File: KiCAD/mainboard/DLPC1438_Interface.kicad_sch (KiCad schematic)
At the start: 81 parts, among them IC1 DLPC1438ZEZ, IC14 SN74AUP1G06DCKR, IC6 SN74AUP1G06DCKR, J2 Conn_01x07_Pin, J3 Conn_02x05_Odd_Even, J31 Conn_01x08_Pin, J4 Conn_01x05_Pin, U12 ECS-2520MV-xxx-xx, U13 MX25L3233FM2, U22 TXS0102DCU, U7 SN74AUP1G06DCKR

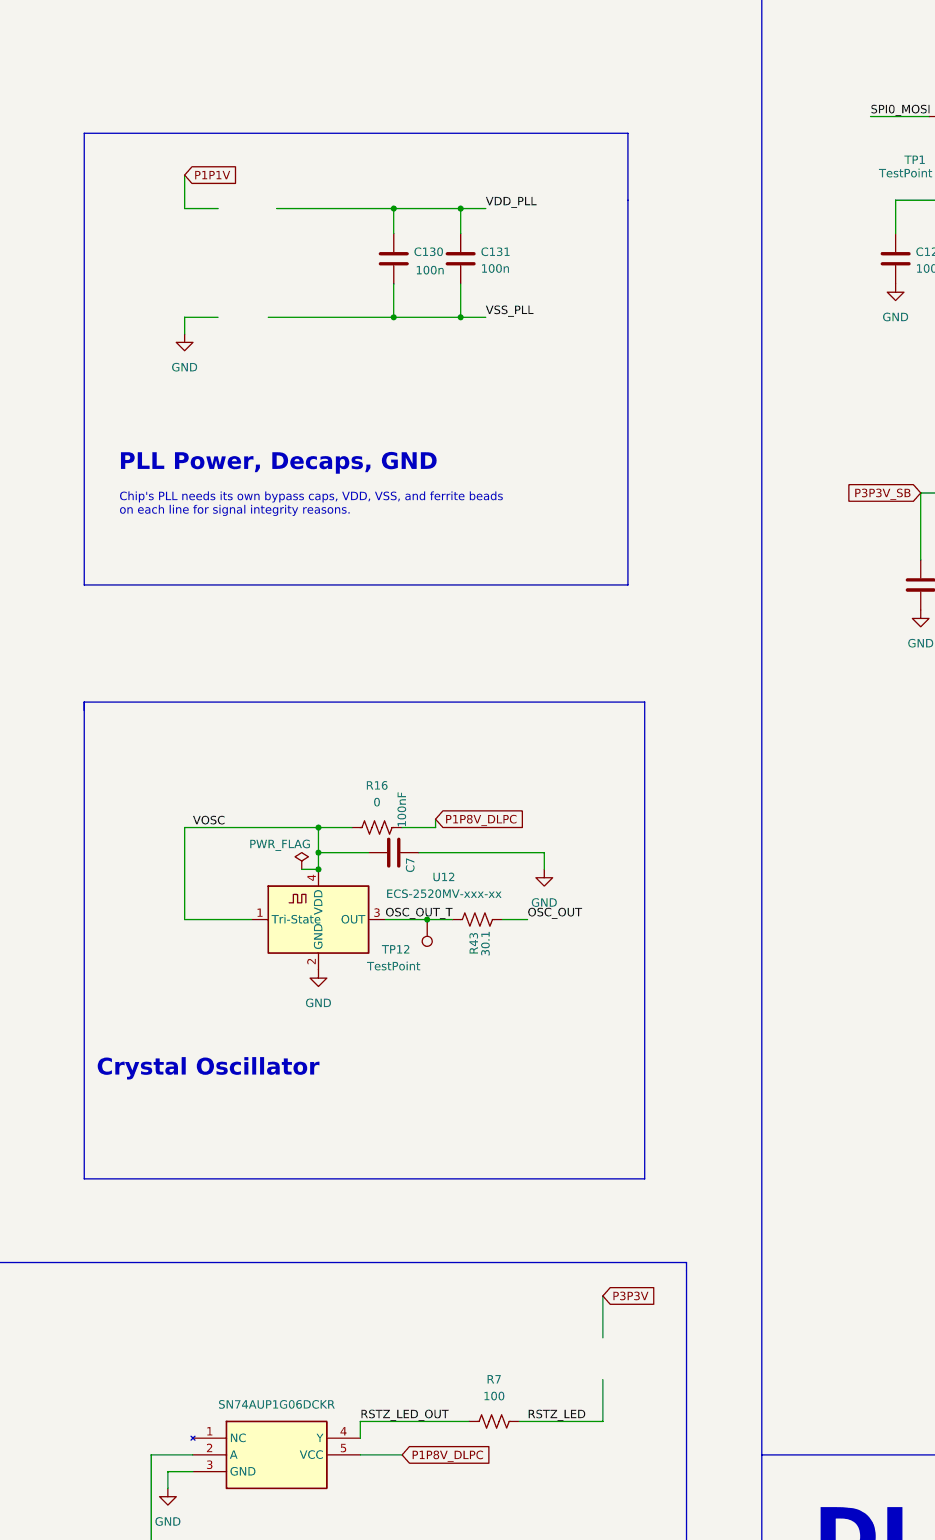
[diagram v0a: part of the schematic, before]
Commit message: added libraries and symbols and step for ferrite beads and D7 LED
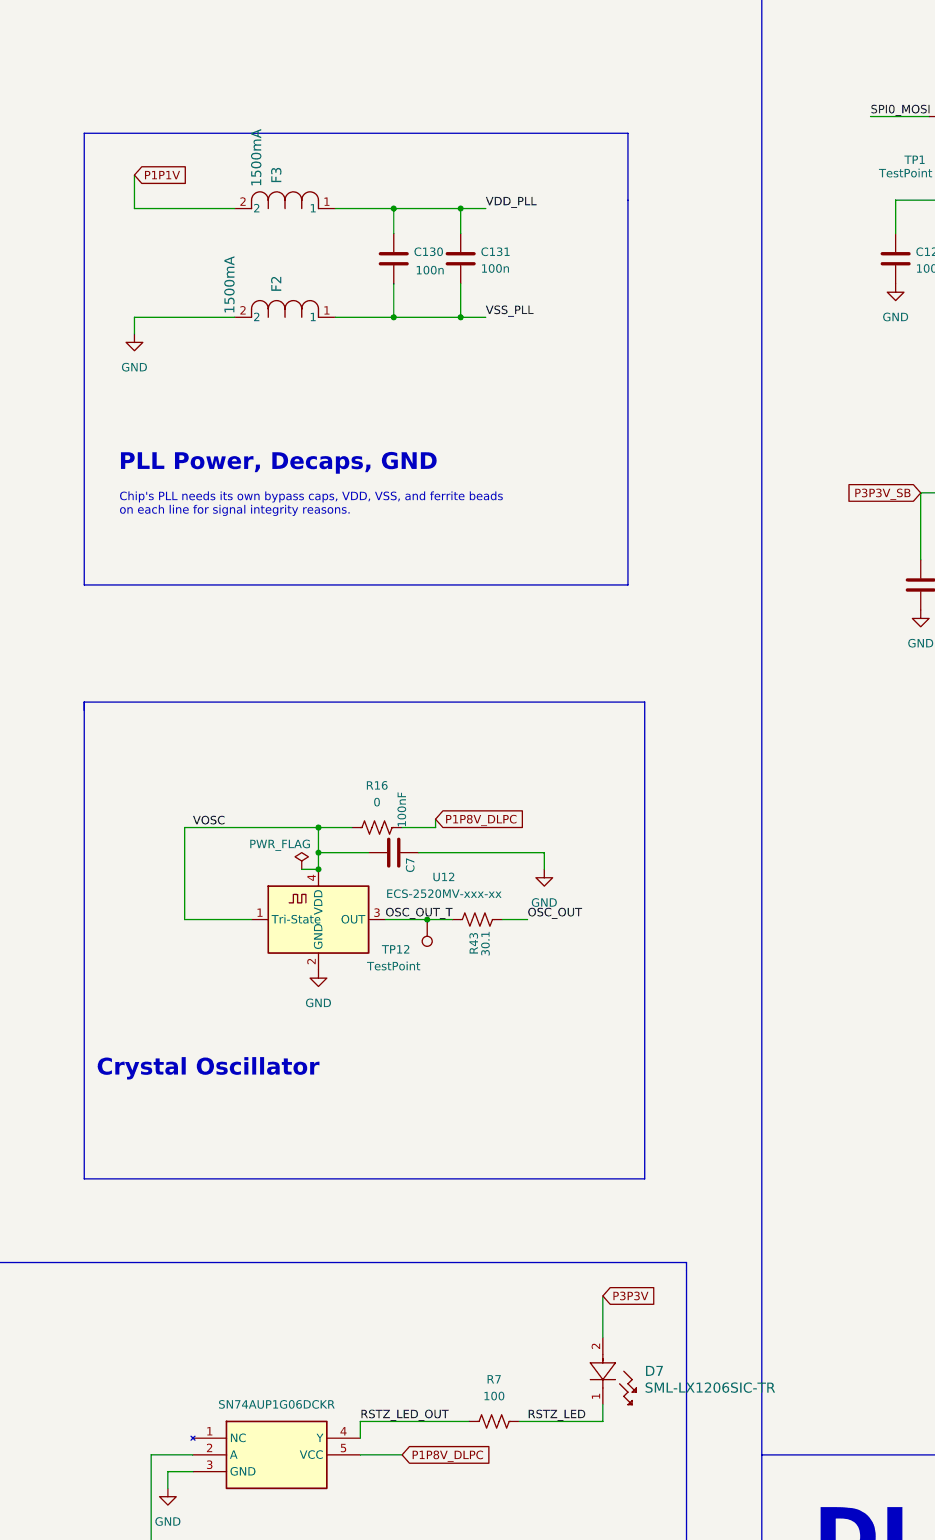
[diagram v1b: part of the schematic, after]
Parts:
- added D7: SML-LX1206SIC-TR, tp_library:LED_SML-LX1206SIC-TR_LUM-M, symbol ul_SML-LX1206SIC-TR:SML-LX1206SIC-TR
- added F2, F3: 1500mA, tp_library:BLM15P_FBD-M, symbol BLM15P_FBD-M:BLM15PD800SN1D
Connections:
- net GND: now also F2.2
- net P1P1V: now also F3.2
- net P3P3V: now also D7.2
- net RSTZ_LED: now also D7.1
- net VDD_PLL: now also F3.1
- net VSS_PLL: now also F2.1
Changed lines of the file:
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@@
 	(wire
 		(pts
-			(xy 210.82 127) (xy 215.9 127)
+			(xy 203.2 127) (xy 218.44 127)
 		)
 		(stroke
@@
 	(wire
 		(pts
-			(xy 224.79 127) (xy 242.57 127)
+			(xy 233.68 127) (xy 242.57 127)
 		)
 		(stroke
@@
 	(wire
 		(pts
-			(xy 274.32 304.8) (xy 274.32 311.15)
-		)
-		(stroke
-			(width 0)
-			(type default)
-		)
-	)
-	(wire
-		(pts
 			(xy 534.67 345.44) (xy 533.4 345.44)
 		)
@@
 	(wire
 		(pts
-			(xy 210.82 143.51) (xy 210.82 146.05)
+			(xy 203.2 143.51) (xy 203.2 146.05)
 		)
 		(stroke
@@
 	(wire
 		(pts
-			(xy 215.9 143.51) (xy 210.82 143.51)
+			(xy 218.44 143.51) (xy 203.2 143.51)
 		)
 		(stroke
@@
 	(wire
 		(pts
+			(xy 274.32 292.1) (xy 274.32 298.45)
+		)
+		(stroke
+			(width 0)
+			(type default)
+		)
+	)
+	(wire
+		(pts
 			(xy 417.83 250.19) (xy 421.64 250.19)
 		)
@@
 	(wire
 		(pts
-			(xy 210.82 121.92) (xy 210.82 127)
+			(xy 203.2 121.92) (xy 203.2 127)
 		)
 		(stroke
@@
 	(wire
 		(pts
-			(xy 431.8 49.53) (xy 431.8 64.77)
+			(xy 274.32 308.61) (xy 274.32 311.15)
 		)
 		(stroke
@@
 	(wire
 		(pts
-			(xy 186.69 60.96) (xy 186.69 66.04)
+			(xy 431.8 49.53) (xy 431.8 64.77)
 		)
 		(stroke
@@
 	(wire
 		(pts
-			(xy 201.93 66.04) (xy 210.82 66.04)
+			(xy 186.69 60.96) (xy 186.69 66.04)
 		)
 		(stroke
@@
 	(wire
 		(pts
-			(xy 513.08 342.9) (xy 510.54 342.9)
+			(xy 201.93 66.04) (xy 210.82 66.04)
 		)
 		(stroke
@@
 		)
 	)
-	(polyline
+	(wire
 		(pts
-			(xy 170.18 273.05) (xy 20.32 273.05)
+			(xy 513.08 342.9) (xy 510.54 342.9)
 		)
 		(stroke
@@
 		)
 	)
-	(wire
+	(polyline
 		(pts
-			(xy 492.76 68.58) (xy 528.32 68.58)
+			(xy 170.18 273.05) (xy 20.32 273.05)
 		)
 		(stroke
@@
 	(wire
 		(pts
-			(xy 274.32 292.1) (xy 274.32 298.45)
+			(xy 492.76 68.58) (xy 528.32 68.58)
 		)
 		(stroke
@@
 	(wire
 		(pts
-			(xy 223.52 143.51) (xy 242.57 143.51)
+			(xy 233.68 143.51) (xy 242.57 143.51)
 		)
 		(stroke
@@
 	(global_label "P1P1V"
 		(shape input)
-		(at 210.82 121.92 0)
+		(at 203.2 121.92 0)
 		(fields_autoplaced yes)
 		(effects
@@
 		)
 		(property "Intersheetrefs" "${INTERSHEET_REFS}"
-			(at 219.8528 121.92 0)
+			(at 212.2328 121.92 0)
 			(effects
 				(font
@@
 	)
 	(symbol
+		(lib_id "BLM15P_FBD-M:BLM15PD800SN1D")
+		(at 218.44 127 270)
+		(unit 1)
+		(exclude_from_sim no)
+		(in_bom yes)
+		(on_board yes)
+		(dnp no)
+		(property "Reference" "F3"
+			(at 224.7899 123.19 0)
+			(effects
+				(font
+					(size 1.524 1.524)
+				)
+				(justify right)
+			)
+		)
+		(property "Value" "1500mA"
+			(at 221.742 123.698 0)
+			(effects
+				(font
+					(size 1.524 1.524)
+				)
+				(justify right)
+			)
+		)
+		(property "Footprint" "tp_library:BLM15P_FBD-M"
+			(at 218.44 127 0)
+			(effects
+				(font
+					(size 1.27 1.27)
+					(italic yes)
+				)
+				(hide yes)
+			)
+		)
+		(property "Datasheet" "BLM15PD800SN1D"
+			(at 218.44 127 0)
+			(effects
+				(font
+					(size 1.27 1.27)
+					(italic yes)
+				)
+				(hide yes)
+			)
+		)
+		(property "Description" ""
+			(at 218.44 127 0)
+			(effects
+				(font
+					(size 1.27 1.27)
+				)
+				(hide yes)
+			)
+		)
+		(pin "1"
+		)
+		(pin "2"
+		)
+		(instances
+			(project ""
+				(path "/38e83f42-2cf9-4799-a46f-ca415d95b90a/a69a407c-1a7c-4ac9-a9eb-cd67809c5ec0"
+					(reference "F3")
+					(unit 1)
+				)
+			)
+		)
+	)
+	(symbol
 		(lib_id "power:GND")
 		(at 330.2 142.24 0)
@@
 	)
 	(symbol
+		(lib_id "BLM15P_FBD-M:BLM15PD800SN1D")
+		(at 218.44 143.51 270)
+		(unit 1)
+		(exclude_from_sim no)
+		(in_bom yes)
+		(on_board yes)
+		(dnp no)
+		(property "Reference" "F2"
+			(at 224.7899 139.7 0)
+			(effects
+				(font
+					(size 1.524 1.524)
+				)
+				(justify right)
+			)
+		)
+		(property "Value" "1500mA"
+			(at 217.678 143.002 0)
+			(effects
+				(font
+					(size 1.524 1.524)
+				)
+				(justify right)
+			)
+		)
+		(property "Footprint" "tp_library:BLM15P_FBD-M"
+			(at 218.44 143.51 0)
+			(effects
+				(font
+					(size 1.27 1.27)
+					(italic yes)
+				)
+				(hide yes)
+			)
+		)
+		(property "Datasheet" "BLM15PD800SN1D"
+			(at 218.44 143.51 0)
+			(effects
+				(font
+					(size 1.27 1.27)
+					(italic yes)
+				)
+				(hide yes)
+			)
+		)
+		(property "Description" ""
+			(at 218.44 143.51 0)
+			(effects
+				(font
+					(size 1.27 1.27)
+				)
+				(hide yes)
+			)
+		)
+		(pin "1"
+		)
+		(pin "2"
+		)
+		(instances
+			(project "mainboard"
+				(path "/38e83f42-2cf9-4799-a46f-ca415d95b90a/a69a407c-1a7c-4ac9-a9eb-cd67809c5ec0"
+					(reference "F2")
+					(unit 1)
+				)
+			)
+		)
+	)
+	(symbol
 		(lib_id "Connector:Conn_01x05_Pin")
 		(at 547.37 124.46 0)
@@
 	)
 	(symbol
+		(lib_id "ul_SML-LX1206SIC-TR:SML-LX1206SIC-TR")
+		(at 274.32 298.45 270)
+		(unit 1)
+		(exclude_from_sim no)
+		(in_bom yes)
+		(on_board yes)
+		(dnp no)
+		(fields_autoplaced yes)
+		(property "Reference" "D7"
+			(at 280.67 303.5299 90)
+			(effects
+				(font
+					(size 1.524 1.524)
+				)
+				(justify left)
+			)
+		)
+		(property "Value" "SML-LX1206SIC-TR"
+			(at 280.67 306.0699 90)
+			(effects
+				(font
+					(size 1.524 1.524)
+				)
+				(justify left)
+			)
+		)
+		(property "Footprint" "tp_library:LED_SML-LX1206SIC-TR_LUM-M"
+			(at 274.32 298.45 0)
+			(effects
+				(font
+					(size 1.27 1.27)
+					(italic yes)
+				)
+				(hide yes)
+			)
+		)
+		(property "Datasheet" "SML-LX1206SIC-TR"
+			(at 274.32 298.45 0)
+			(effects
+				(font
+					(size 1.27 1.27)
+					(italic yes)
+				)
+				(hide yes)
+			)
+		)
+		(property "Description" ""
+			(at 274.32 298.45 0)
+			(effects
+				(font
+					(size 1.27 1.27)
+				)
+				(hide yes)
+			)
+		)
+		(pin "2"
+		)
+		(pin "1"
+		)
+		(instances
+			(project ""
+				(path "/38e83f42-2cf9-4799-a46f-ca415d95b90a/a69a407c-1a7c-4ac9-a9eb-cd67809c5ec0"
+					(reference "D7")
+					(unit 1)
+				)
+			)
+		)
+	)
+	(symbol
 		(lib_id "Device:C")
 		(at 210.82 57.15 0)
@@
 	(symbol
 		(lib_id "power:GND")
-		(at 210.82 146.05 0)
+		(at 203.2 146.05 0)
 		(unit 1)
 		(exclude_from_sim no)
@@
 		(fields_autoplaced yes)
 		(property "Reference" "#PWR032"
-			(at 210.82 152.4 0)
+			(at 203.2 152.4 0)
 			(effects
 				(font
@@
 		)
 		(property "Value" "GND"
-			(at 210.82 151.13 0)
+			(at 203.2 151.13 0)
 			(effects
 				(font
@@
 		)
 		(property "Footprint" ""
-			(at 210.82 146.05 0)
+			(at 203.2 146.05 0)
 			(effects
 				(font
@@
 		)
 		(property "Datasheet" ""
-			(at 210.82 146.05 0)
+			(at 203.2 146.05 0)
 			(effects
 				(font
@@
 		)
 		(property "Description" "Power symbol creates a global label with name \"GND\" , ground"
-			(at 210.82 146.05 0)
+			(at 203.2 146.05 0)
 			(effects
 				(font

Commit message: added sym mod and step for resistors but package 0805
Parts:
- removed R1: 10k, Resistor_SMD:R_0805_2012Metric_Pad1.20x1.40mm_HandSolder, symbol Device:R_US
- removed R3: 100k, Resistor_SMD:R_0805_2012Metric_Pad1.20x1.40mm_HandSolder, symbol Device:R_US
- added R1: 10k, tp_library:STA_RMCF0805_STP-M, symbol RMCF0805FT10K0:RMCF0805FT10K0
- added R8: 100, tp_library:RES_CRCW_0805-M, symbol CRCW0805100RFKEA:CRCW0805100RFKEA
- added R9: 30.1, RC0805FR-0730R1L:RESC2012X60N, symbol RC0805FR-0730R1L:RC0805FR-0730R1L
- C112, C114, C115, C170, C171, C7: value 100nF -> 100n; footprint Capacitor_SMD:C_0805_2012Metric_Pad1.18x1.45mm_HandSolder -> Capacitor_SMD:C_0402_1005Metric; Manufacturer_Part_Number (none) -> CL05B104KO5NNNC
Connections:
- net GND: now also C115.1, C170.2, C171.1, C7.1; no longer C115.2, C170.1, C171.2, C7.2
- net P1P8V_DLPC: now also C170.1; no longer C170.2
- net P3P3V: now also C171.2; no longer C171.1
- net P3P3V_SB: now also C115.2; no longer C115.1
- net VOSC: now also C7.2; no longer C7.1

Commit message: replaced with 0805 all passives in DLPC
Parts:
- removed R1: 10k, tp_library:STA_RMCF0805_STP-M, symbol RMCF0805FT10K0:RMCF0805FT10K0
- removed R2: 100, Resistor_SMD:R_0805_2012Metric_Pad1.20x1.40mm_HandSolder, symbol Device:R_US
- removed R8: 100, tp_library:RES_CRCW_0805-M, symbol CRCW0805100RFKEA:CRCW0805100RFKEA
- removed R9: 30.1, RC0805FR-0730R1L:RESC2012X60N, symbol RC0805FR-0730R1L:RC0805FR-0730R1L
- C112, C114, C115, C120, C121, C125, C126, C127, C128, C129, C130, C131, C132, C133, C134, C138, C139, C140, C141, C142, C143, C144, C145, C155, C156, C157, C170, C171, C7: footprint Capacitor_SMD:C_0402_1005Metric -> CC0805KRX7R9BB104:CAPC2012X70; symbol Device:C -> CC0805KRX7R9BB104:CC0805KRX7R9BB104; Check_prices (none) -> https://www.snapeda.com/parts/CC0805KRX7R9BB104/Yageo/view-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; Description_1 (none) -> 0.1 µF ±10% 50V Ceramic Capacitor X7R 0805 (2012 Metric); DigiKey_Part_Number (none) -> 311-1140-1-ND; MANUFACTURER (none) -> YAGEO; MF (none) -> Yageo; MP (none) -> CC0805KRX7R9BB104; Package (none) -> 0805 Yageo; SnapEDA_Link (none) -> https://www.snapeda.com/parts/CC0805KRX7R9BB104/Yageo/view-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
- R16, R171: footprint Resistor_SMD:R_0805_2012Metric_Pad1.20x1.40mm_HandSolder -> RES_R-070RL_VIS; symbol Device:R_US -> RC0805JR-070RL:RC0805JR-070RL; Manufacturer_Part_Number (none) -> RC0805JR-070RL
- R163, R164, R165, R170, R92: footprint Resistor_SMD:R_0805_2012Metric_Pad1.20x1.40mm_HandSolder -> STA_RMCF0805_STP; symbol Device:R_US -> RMCF0805FT10K0:RMCF0805FT10K0; Manufacturer_Part_Number (none) -> RMCF0805FT10K0
- R166: footprint Resistor_SMD:R_0402_1005Metric -> STA_RMCF0805_STP; symbol Device:R_US -> RMCF0805FT10K0:RMCF0805FT10K0; Manufacturer_Part_Number CRCW0402100KFKED -> RMCF0805FT10K0
- R168, R17, R174, R19: footprint Resistor_SMD:R_0805_2012Metric_Pad1.20x1.40mm_HandSolder -> RES_RMCF0805_STP; symbol Device:R_US -> RMCF0805FG100K:RMCF0805FG100K; Manufacturer_Part_Number (none) -> RMCF0805FG100K
- R172, R173, R18, R43, R76: footprint Resistor_SMD:R_0805_2012Metric_Pad1.20x1.40mm_HandSolder -> RC0805FR-0730R1L:RESC2012X60N; symbol Device:R_US -> RC0805FR-0730R1L:RC0805FR-0730R1L; Check_prices (none) -> https://www.snapeda.com/parts/RC0805FR-0730R1L/Yageo/view-p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; Description_1 (none) -> 30.1 Ohms ±1% 0.125W, 1/8W Chip Resistor 0805 (2012 Metric)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; DigiKey_Part_Number (none) -> 311-30.1CRCT-ND; MF (none) -> Yageo; MP (none) -> RC0805FR-0730R1L; Manufacturer_Part_Number (none) -> RC0805FR-0730R1L; Package (none) -> 2012 Yageo; SnapEDA_Link (none) -> https://www.snapeda.com/parts/RC0805FR-0730R1L/Yageo/view-p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
- R176, R177, R178, R179: footprint Resistor_SMD:R_0402_1005Metric -> RES_RMCF0805_STP; symbol Device:R_US -> RMCF0805FG100K:RMCF0805FG100K; Manufacturer_Part_Number CRCW0402100KFKED -> RMCF0805FG100K
- R42, R52: footprint Resistor_SMD:R_0402_1005Metric -> RES_RM10_CCE; symbol Device:R_US -> RM10F7871CT:RM10F7871CT
- R5, R7: footprint Resistor_SMD:R_0805_2012Metric_Pad1.20x1.40mm_HandSolder -> RES_CRCW_0805; symbol Device:R_US -> CRCW0805100RFKEA:CRCW0805100RFKEA; Manufacturer_Part_Number (none) -> CRCW0805100RFKEA
- R53, R54, R55, R73: footprint Resistor_SMD:R_0805_2012Metric_Pad1.20x1.40mm_HandSolder -> RES_ERJP06_PAN; symbol Device:R_US -> ERJP06F3301V:ERJP06F3301V
- R74, R75, R77: footprint RC0402FR-0730R1L -> RC0805FR-0730R1L:RESC2012X60N; symbol Device:R_US -> RC0805FR-0730R1L:RC0805FR-0730R1L; Check_prices (none) -> https://www.snapeda.com/parts/RC0805FR-0730R1L/Yageo/view-p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; Description_1 (none) -> 30.1 Ohms ±1% 0.125W, 1/8W Chip Resistor 0805 (2012 Metric)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; DigiKey_Part_Number (none) -> 311-30.1CRCT-ND; MF (none) -> Yageo; MP (none) -> RC0805FR-0730R1L; Manufacturer_Part_Number RC0402FR-0730R1L -> RC0805FR-0730R1L; Package (none) -> 2012 Yageo; SnapEDA_Link (none) -> https://www.snapeda.com/parts/RC0805FR-0730R1L/Yageo/view-p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
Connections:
- net DLPC_FLSH_PROG: now also R163.1; no longer R163.2, R165.1
- net GND: now also C121.1, C129.1, C133.1, C134.1, C144.1, C145.1, R164.1, R165.1, R174.1, R177.2, R178.2, R179.2, R19.1; no longer C112.2, C114.1, C115.1, C120.2, C121.2, C125.2, C126.2, C127.2, C128.2, C129.2, C132.2, C133.2, C134.2, C138.2, C139.2, C140.2, C141.2, C142.2, C143.2, C144.2, C145.2, C155.2, C156.2, C157.2, C170.2, C171.1, C7.1, R164.2, R165.2, R174.2, R178.1, R179.1, R19.2
- net I2C1_33_EN: no longer R92.2, U22.6 (OE)
- net JTAG_TRSTZ: now also R164.2; no longer R164.1
- net P1P1V: no longer C120.1, C125.1, C126.1, C127.1, C128.1, C132.1, C139.1, C140.1, C141.1, C142.1, C143.1, C155.1
- net P1P8V_DLPC: now also C121.2, C129.2, C133.2, C134.2, C144.2, C145.2; no longer C112.1, C114.2, C121.1, C129.1, C133.1, C134.1, C144.1, C145.1, C156.1, C157.1, C170.1, R177.2
- net P3P3V: now also R5.1; no longer C171.2, R5.2
- net P3P3V_SB: no longer C115.2, C138.1
- net RSTZ_LED: now also R7.1; no longer R7.2
- net RSTZ_LED_OUT: now also R7.2; no longer R7.1
- net SPI0_5V: now also R163.2; no longer R163.1
- net SPI0_CLK: now also R19.2; no longer R19.1
- net SPI0_MOSI: now also R165.2
- net SPI1_MISO: now also R179.1; no longer R179.2
- net SPI1_MOSI: now also R178.1; no longer R178.2
- net VDD_PLL: no longer C130.1, C131.1
- net VOSC: no longer C7.2
- net VSS_PLL: no longer C130.2, C131.2
- net at R171.2, TP21.1: now also R174.2; no longer R174.1
- net at IC6.4 (Y): now also R5.2; no longer R5.1
- new net: R92.2, U22.6 (OE)
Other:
- moved on the sheet: TP21

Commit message: capacitors placed back in place
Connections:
- net GND: now also C112.1, C115.2, C120.1, C125.1, C126.1, C127.1, C128.1, C132.1, C139.1, C140.1, C141.1, C142.1, C143.1, C155.1, C156.1, C157.1, C170.1, C171.2, C7.2
- net P1P1V: now also C120.2, C125.2, C126.2, C127.2, C128.2, C132.2, C139.2, C140.2, C141.2, C142.2, C143.2, C155.2
- net P1P8V_DLPC: now also C112.2, C156.2, C157.2, C170.2
- net P3P3V: now also C171.1
- net P3P3V_SB: now also C115.1
- net VDD_PLL: now also C130.2, C131.2
- net VOSC: now also C7.1
- net VSS_PLL: now also C130.1, C131.1
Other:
- moved on the sheet: C112, C115, C120, C125, C126, C127, C128, C130, C131, C132, C138, C139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

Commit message: changes to all schematic files fixing ERC errors
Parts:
- added R171: 0, RES_R-070RL_VIS, symbol RC0805JR-070RL:RC0805JR-070RL
- added R174: 100k, RES_RMCF0805_STP, symbol RMCF0805FG100K:RMCF0805FG100K
- renumbered TP1 to TP20, IC1 to U16
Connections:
- net DLPC_LED_SEL_1: now also R171.2
- net GND: now also C114.2, C138.1, R174.1; no longer R177.2
- net GPIO_3: now also R177.2
- net I2C1_33_EN: now also R92.2, U22.6 (OE)
- net LED_SEL_1: now also R171.1, R174.2
- net P1P8V_DLPC: now also C114.1, R177.1
- net P3P3V_SB: now also C138.2
- net SPI1_CSZ0: no longer R177.1
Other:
- moved on the sheet: C114, C138, R177, R178, R75

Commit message: more ERC knocked out
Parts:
- removed R171: 0, RES_R-070RL_VIS, symbol RC0805JR-070RL:RC0805JR-070RL
- removed R174: 100k, RES_RMCF0805_STP, symbol RMCF0805FG100K:RMCF0805FG100K
- removed TP20: TestPoint, TestPoint:TestPoint_Pad_D1.5mm, symbol Connector:TestPoint
- added C108, C238, C239: 100n, CC0805KRX7R9BB104:CAPC2012X70, symbol CC0805KRX7R9BB104:CC0805KRX7R9BB104
- added J10: Conn_01x05_Pin, Connector_PinHeader_2.54mm:PinHeader_1x05_P2.54mm_Vertical, symbol Connector:Conn_01x05_Pin
- added J29: Conn_01x04_Pin, Connector_PinHeader_2.54mm:PinHeader_1x04_P2.54mm_Vertical, symbol Connector:Conn_01x04_Pin
- added R155, R158: 10k, STA_RMCF0805_STP, symbol RMCF0805FT10K0:RMCF0805FT10K0
- added R156, R157, R8: 0, RES_R-070RL_VIS, symbol RC0805JR-070RL:RC0805JR-070RL
- added TP14: TestPoint, symbol Connector:TestPoint
- added U37: TXS0102DCU, Package_SO:VSSOP-8_2.3x2mm_P0.5mm, symbol Logic_LevelTranslator:TXS0102DCU
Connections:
- net DLC_LED_SEL_1 is gone; now on net DLPC_LED_SEL_1: R171.1
- net DLPC_PLLO: now also TP14.1
- net GND: now also C108.1, C238.1, C239.1, J10.1 (Pin_1), J29.2 (Pin_2), U37.2 (GND)
- net IIC0_SCL: now also U37.5 (A1)
- net IIC0_SDA: now also U37.4 (A2)
- net LED_SEL_1: now also R171.2, R174.2, TP21.1; no longer U16.A12 (CMP_OUT)
- net P3P3V_SB: now also R8.1
- net SPI1_CLK: now also J10.5 (Pin_5)
- net SPI1_CSZ0: now also J10.4 (Pin_4)
- net SPI1_MISO: now also J10.2 (Pin_2)
- net SPI1_MOSI: now also J10.3 (Pin_3)
- new net CMP_OUT: U16.A12 (CMP_OUT)
- new net EXT_I2CPWR: C108.2, J29.1 (Pin_1)
- new net EXT_I2CPWR_F: C239.2, R155.2, R158.2, R8.2, U37.6 (OE), U37.7 (VCCB)
- new net EXT_SCL: J29.3 (Pin_3), R156.1
- new net EXT_SCL_T: R155.1, R156.2, U37.8 (B1)
- new net EXT_SDA: J29.4 (Pin_4), R157.1
- new net EXT_SDA_T: R157.2, R158.1, U37.1 (B2)
- new net P1P8V: C238.2, U37.3 (VCCA)
- no-connect marks 18 -> 22
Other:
- note added: "IICO EXT CONNECTION"
- note added: "SPI external testing"
- note added: "these two resistors are DNI"
- note added: "this is supposed to be a connector not a header"
- note removed: "SPI external connections"
